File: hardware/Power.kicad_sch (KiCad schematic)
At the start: 6 parts, among them J6 1881448, U5 AMS1117-3.3

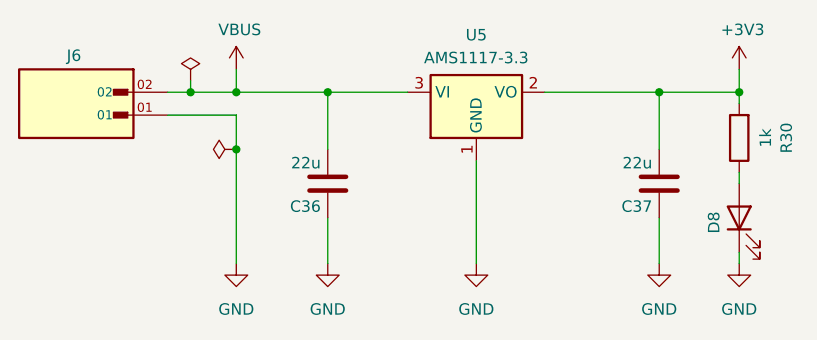
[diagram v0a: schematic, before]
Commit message: fix: status LED resistor value
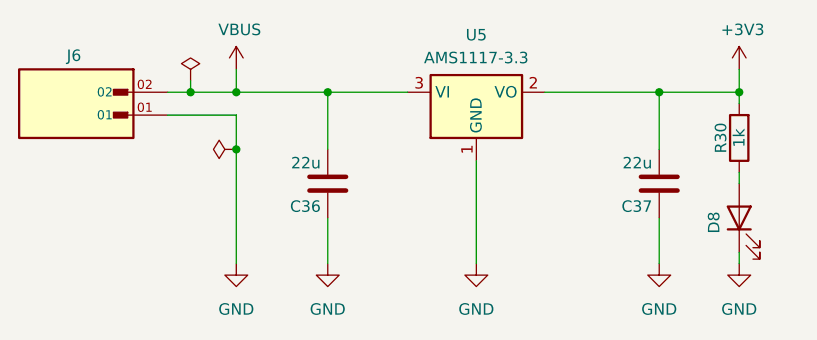
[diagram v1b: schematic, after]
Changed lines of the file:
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@@
 		(dnp no)
 		(property "Reference" "R30"
-			(at 179.2478 101.6 90)
+			(at 171.958 101.6 90)
 			(effects
 				(font
@@
 		)
 		(property "Value" "1k"
-			(at 176.9364 101.6 90)
+			(at 173.99 101.6 90)
 			(effects
 				(font
